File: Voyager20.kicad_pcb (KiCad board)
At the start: 2 copper layers, 73 x 119.1 mm, 104 parts, among them Q1 Q_NPN_BEC, SW1 SW_Push, U1 ATmega32U2-AU, U2 PRTR5V0U2X, Y1 16MHz

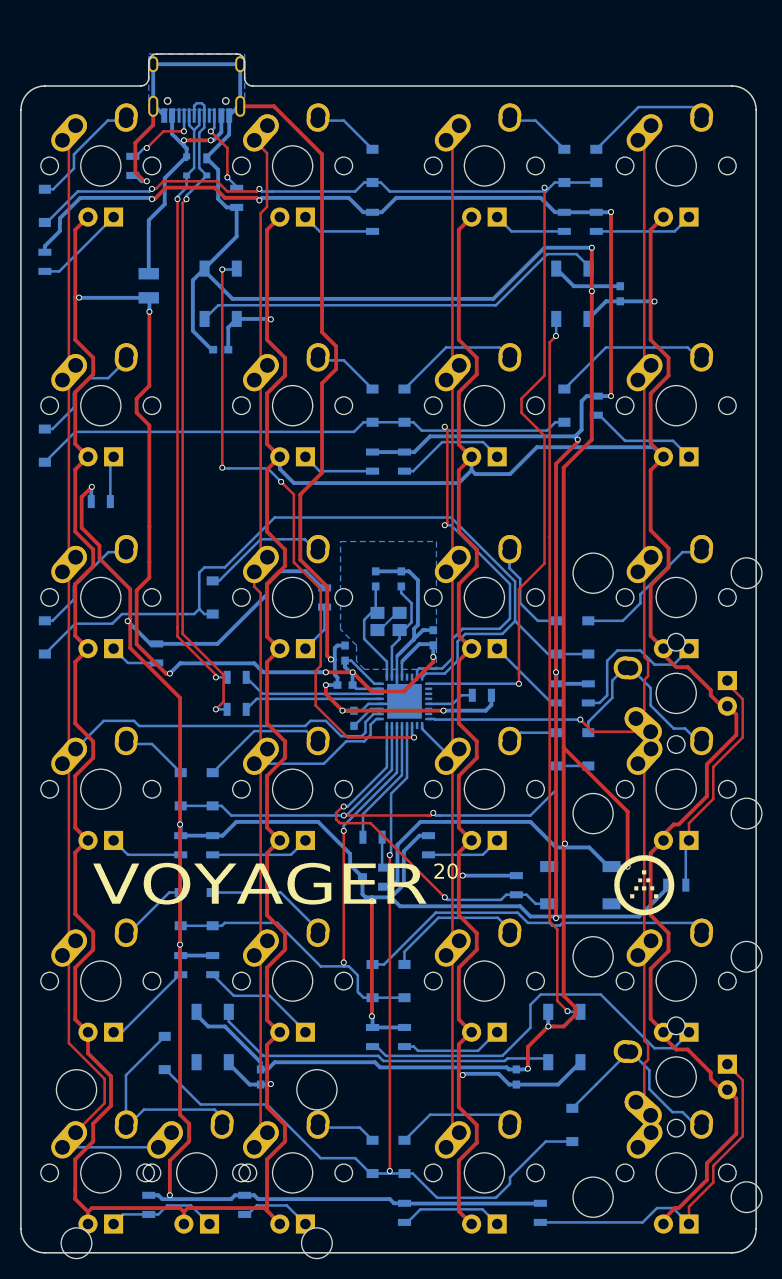
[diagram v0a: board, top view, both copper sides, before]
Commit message: Move Usb
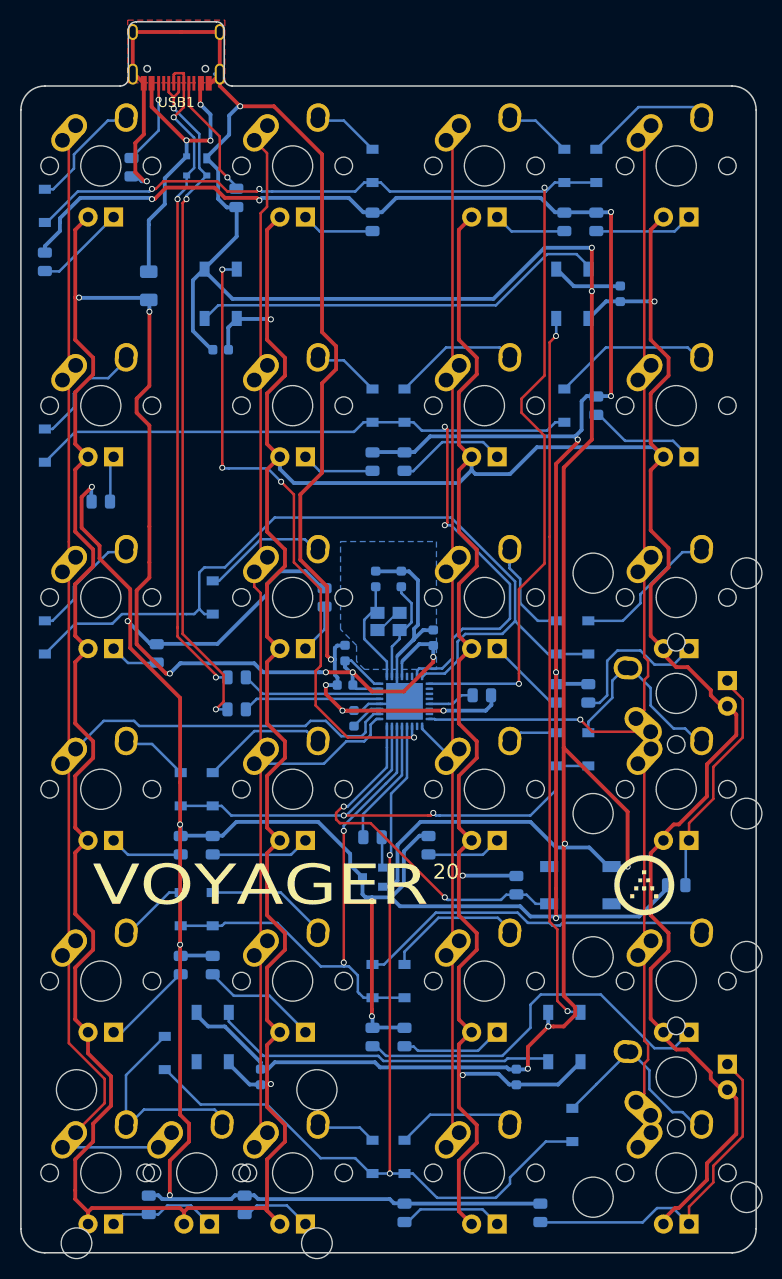
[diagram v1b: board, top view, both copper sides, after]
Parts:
- C1, C2, C3, C4, C5, C6, CR1, CR2, CR3, CR4: footprint Capacitors_SMD:C_0603 -> Capacitor_SMD:C_0603_1608Metric
- D1, D10, D11, D12, D13, D14, D15, D16, D17, D19, D2, D20, D21, D22, D25, D26, D27, D28, D3, D4, D5, D6, D7, D8: footprint Diodes_SMD:D_SOD-123 -> Diode_SMD:D_SOD-123
- D18, D23, D24, D9: footprint LEDs:LED_WS2812B-PLCC4 -> LED_SMD:LED_WS2812B_PLCC4_5.0x5.0mm_P3.2mm
- F1: footprint Fuse_Holders_and_Fuses:Fuse_SMD1206_Reflow -> Fuse:Fuse_1206_3216Metric
- Q1: footprint TO_SOT_Packages_SMD:SOT-23 -> Package_TO_SOT_SMD:SOT-23
- R1, R10, R11, R12, R13, R14, R15, R16, R17, R18, R19, R2, R20, R21, R22, R23, R24, R25, R26, R27, R28, R29, R3, R30, R31, R4, R5, R6, R7, R8, R9: footprint Resistors_SMD:R_0805 -> Resistor_SMD:R_0805_2012Metric
- U1: footprint Housings_DFN_QFN:QFN-32-1EP_5x5mm_Pitch0.5mm -> Package_DFN_QFN:QFN-32-1EP_5x5mm_P0.5mm_EP3.65x3.65mm
- USB1: moved to F.Cu
- Y1: footprint Crystals:Crystal_SMD_3225-4pin_3.2x2.5mm -> Crystal:Crystal_SMD_3225-4Pin_3.2x2.5mm
- moved R4 10.9 mm to (50.7, 16.0)
- moved R6 10.8 mm to (61.1, 19.1)
- moved USB1 3.79 mm to (55.1, -0.03), turned to 180 degrees
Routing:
- net GND: track 396.1 -> 403.7 mm, vias 11 -> 12
- net VCC: track 24.8 -> 30.5 mm, vias 2 -> 3
- net Net-(R2-Pad2): track 61.0 -> 66.6 mm, vias 2 -> 3
- net Net-(R6-Pad1): track 7.69 -> 12.4 mm, vias 2 -> 1
- net Net-(R3-Pad1): track 66.7 -> 69.4 mm, vias 2 -> 3
- net Net-(R4-Pad1): track 8.44 -> 8.32 mm, vias 2 -> 1
- added copper zone on F.Cu, net GND
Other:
- board size 73 x 119.1 mm -> 73 x 122.3 mm
- board text added: "Voyager20 PCB Beurier Edition Modified by @druz320 github.com/aaarsene/Voyager20"
- board text removed: "Voyager20 PCB Rev 1.0 20190126 kb.ai03.me"
